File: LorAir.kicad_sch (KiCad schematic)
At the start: 39 parts, among them U1 STM32WL55JCIx, U2 BGS12WN6E6327

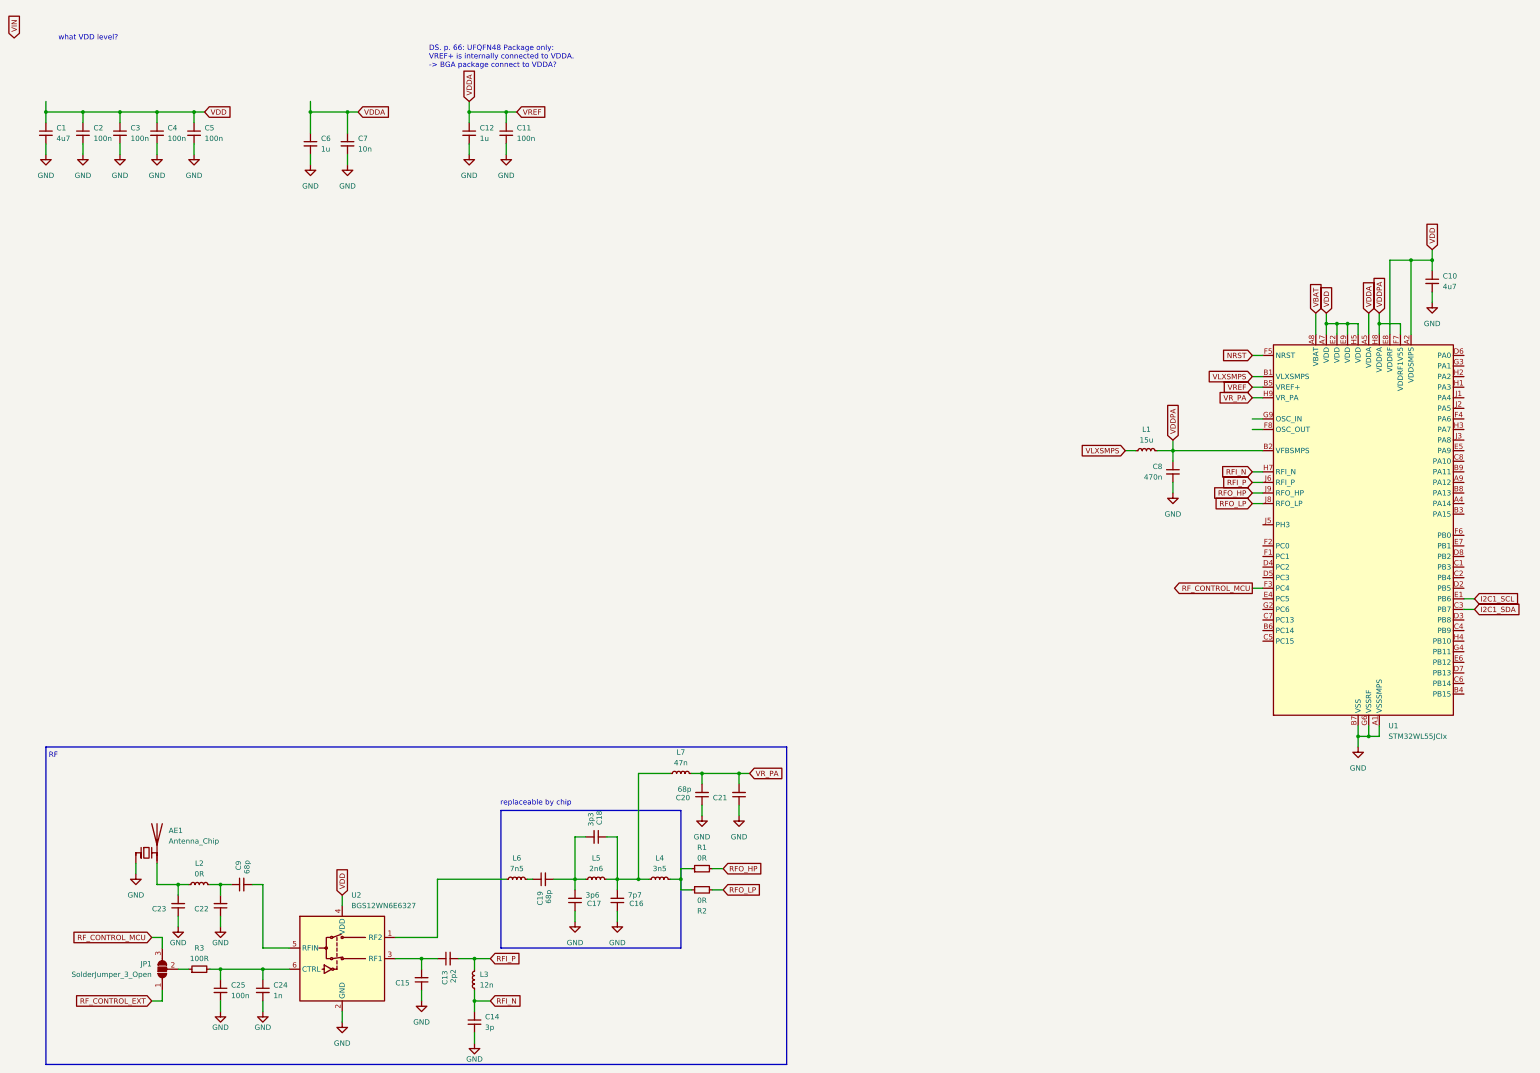
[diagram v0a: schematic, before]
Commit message: Add BME280/680 + Capacitive Soil Moisture Sensor
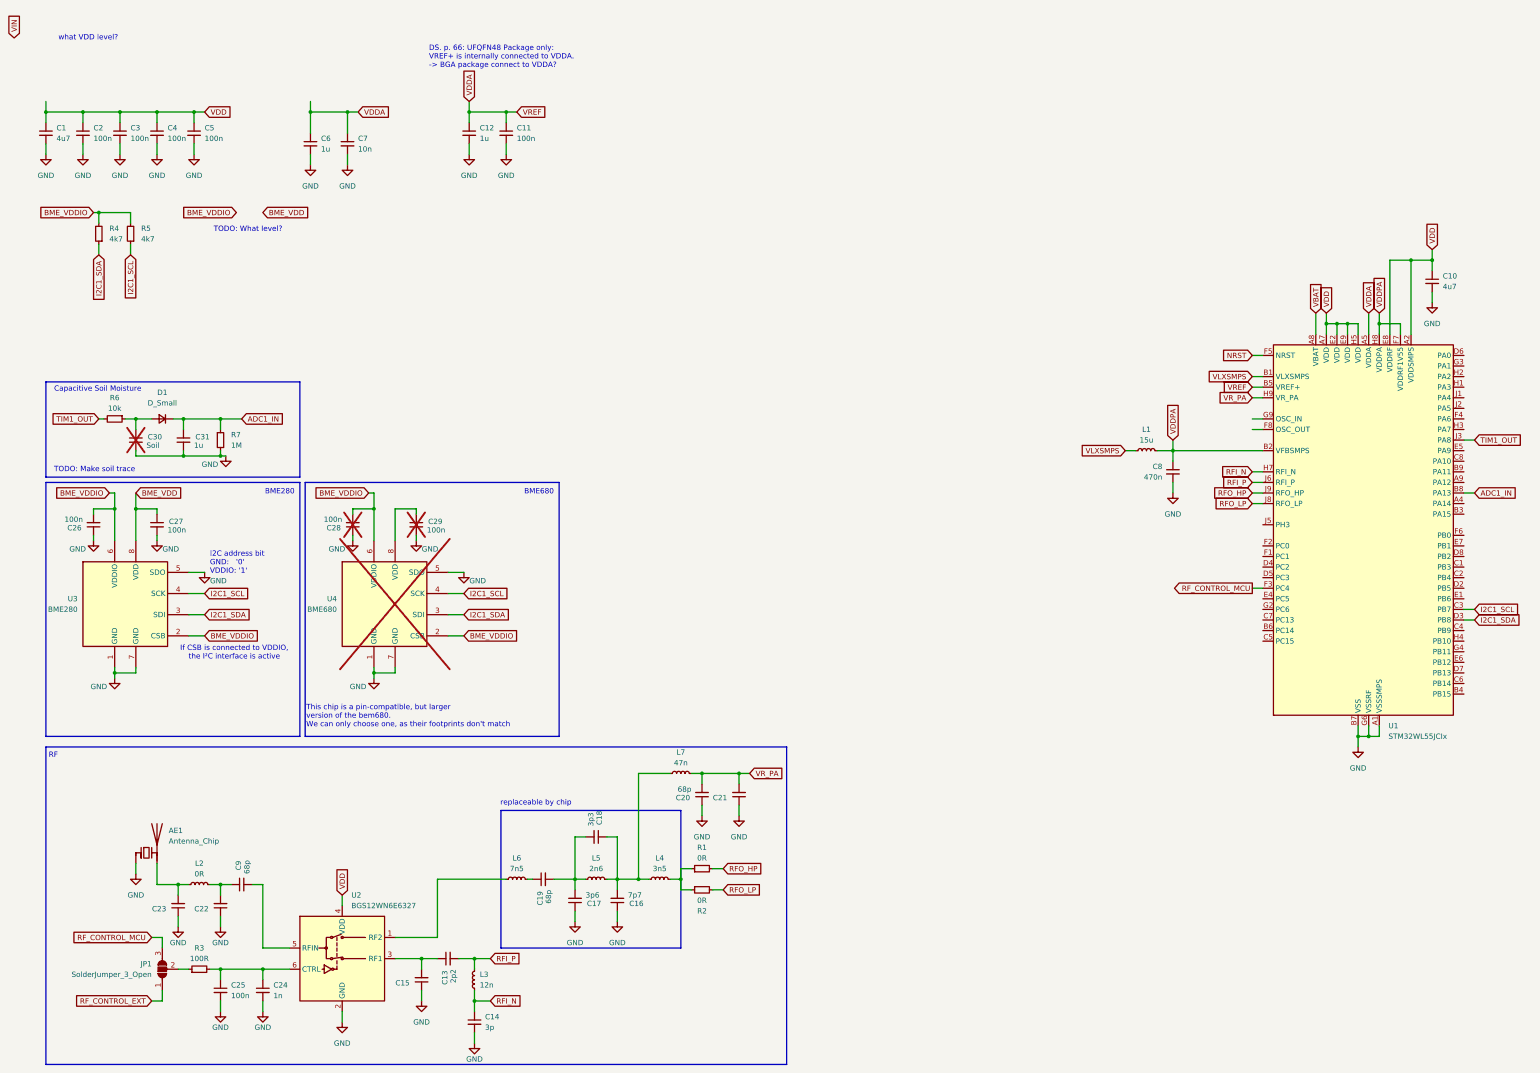
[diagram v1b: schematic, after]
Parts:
- added C26, C27, C28, C29: 100n, Capacitor_SMD:C_0402_1005Metric, symbol Device:C_Small
- added C30: Soil, Capacitor_SMD:C_0402_1005Metric, symbol Device:C_Small
- added C31: 1u, Capacitor_SMD:C_0402_1005Metric, symbol Device:C_Small
- added D1: D_Small, symbol Device:D_Small
- added R4, R5: 4k7, Resistor_SMD:R_0402_1005Metric, symbol Device:R_Small
- added R6: 10k, Resistor_SMD:R_0402_1005Metric, symbol Device:R_Small
- added R7: 1M, Resistor_SMD:R_0402_1005Metric, symbol Device:R_Small
- added U3: BME280, Package_LGA:Bosch_LGA-8_2.5x2.5mm_P0.65mm_ClockwisePinNumbering, symbol Sensor:BME280
- added U4: BME680, Package_LGA:Bosch_LGA-8_3x3mm_P0.8mm_ClockwisePinNumbering, symbol Sensor:BME680
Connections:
- net GND: now also C26.1, C27.2, C28.1, C29.2, C30.2, C31.2, R7.2, U3.1 (GND), U3.5 (SDO), U3.7 (GND), U4.1 (GND), U4.5 (SDO), U4.7 (GND)
- net I2C1_SCL: now also U1.C3 (PB7), R5.1, U3.4 (SCK), U4.4 (SCK); no longer U1.E1 (PB6)
- net I2C1_SDA: now also U1.D3 (PB8), R4.1, U3.3 (SDI), U4.3 (SDI); no longer U1.C3 (PB7)
- net ADC1_IN: now reaches U1.B8 (PA13)
- net ADC1_IN: now also C31.1, D1.1 (K), R7.1
- net TIM1_OUT: now reaches U1.J3 (PA8)
- net TIM1_OUT: now also R6.2
- new net: C30.1, D1.2 (A), R6.1
- new net: C29.1, U4.8 (VDD)
- new net BME_VDD: C27.1, U3.8 (VDD)
- new net BME_VDDIO: C26.2, C28.2, R4.2, R5.2, U3.2 (CSB), U3.6 (VDDIO), U4.2 (CSB), U4.6 (VDDIO)
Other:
- note added: "BME280"
- note added: "BME680"
- note added: "Capacitive Soil Moisture"
- note added: "I2C address bit GND: '0' VDDIO: '1'"
- note added: "If CSB is connected to VDDIO, the I²C interface is active"
- note added: "TODO: Make soil trace"
- note added: "TODO: What level?"
- note added: "This chip is a pin-compatible, but larger version of the bem680. We can only choose one, as their footprints don't match"
